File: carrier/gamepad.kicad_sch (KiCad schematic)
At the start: 57 parts, among them SW1 SKRRACE010, SW10 SKRBAAE010, SW11 SW_Push, SW12 SW_DIP_x04, SW2 SKRRACE010, SW3 SKRRACE010, SW4 SKRRACE010, SW5 SKRRACE010, SW6 SKRRACE010, SW7 SKRBAAE010, SW8 SKRBAAE010, SW9 SW_Push, U1 SN74HC14N

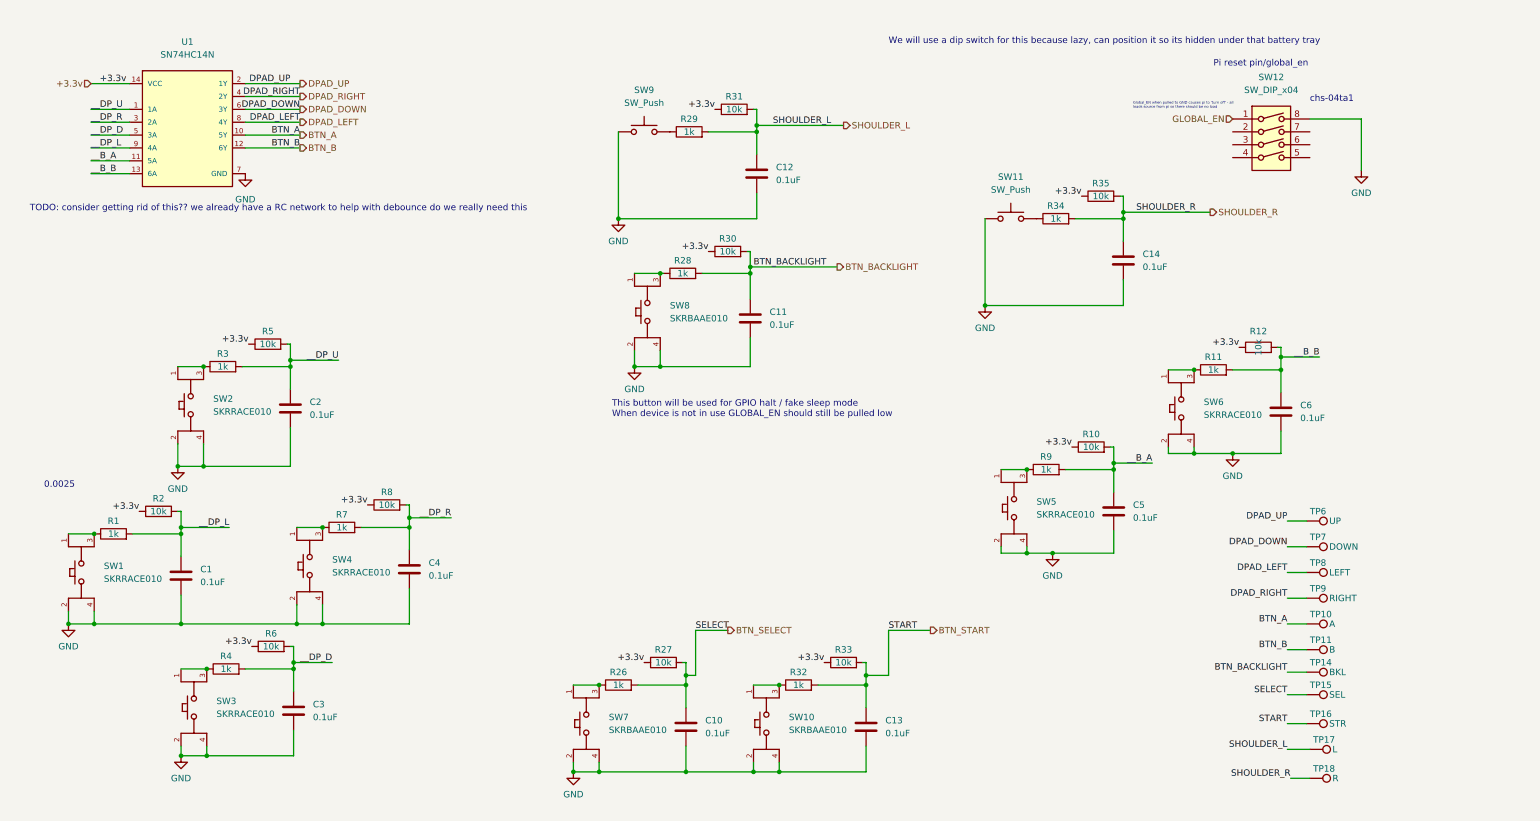
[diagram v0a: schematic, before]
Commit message: getting back into the swing of this
aded some stuff for the resistors, moved some stuff about, removed the schmitt inverter (software is the solution for all our problems, forever)
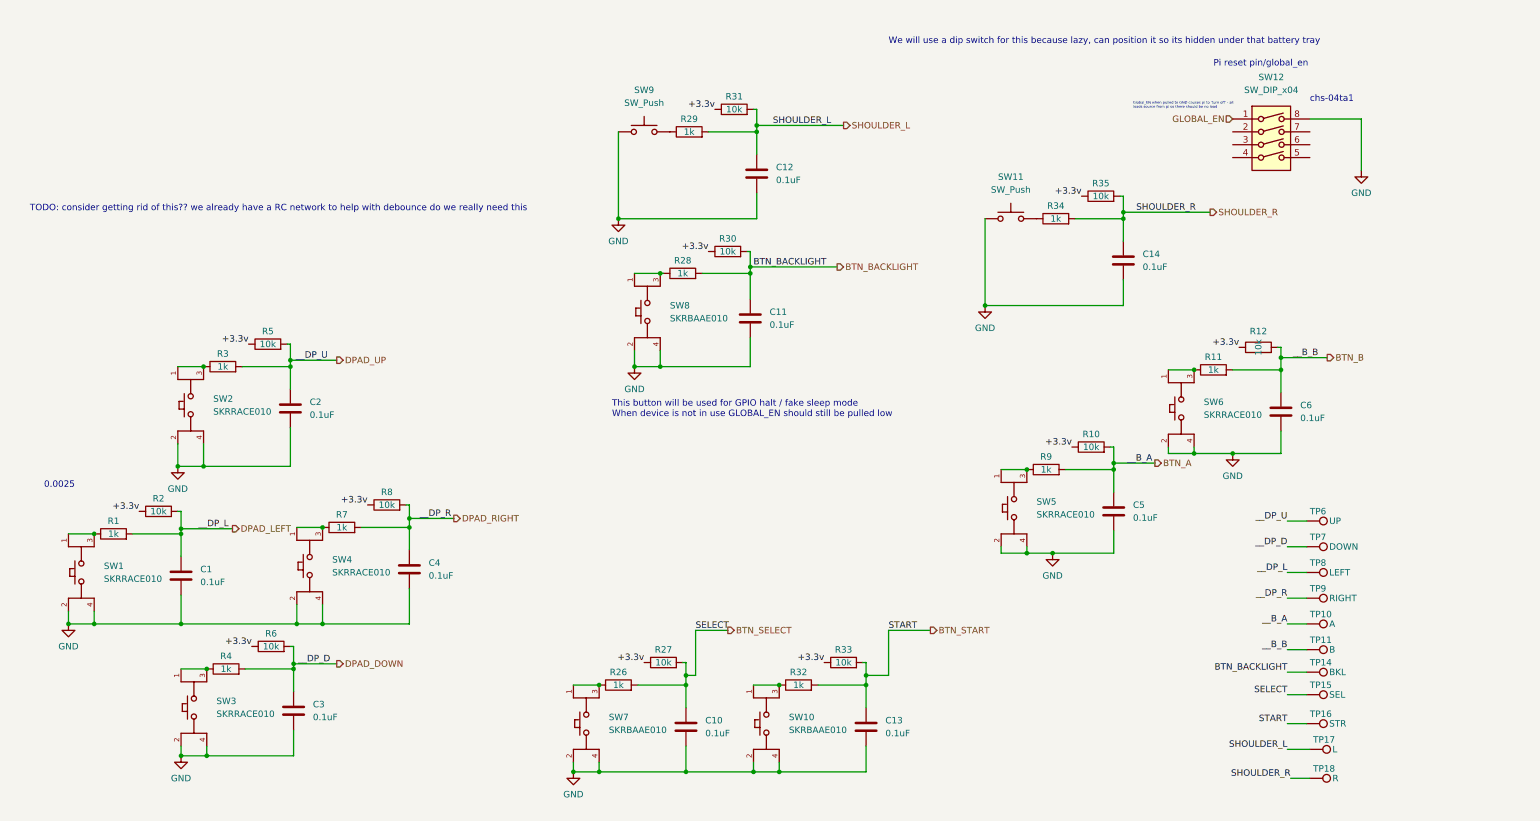
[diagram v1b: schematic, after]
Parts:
- removed U1: SN74HC14N, Package_SO:SO-14_3.9x8.65mm_P1.27mm, symbol TI74HC14N:SN74HC14N
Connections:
- net __B_A is gone; now on net BTN_A: C5.1, R10.2, R9.2
- net __B_B is gone; now on net BTN_B: C6.1, R11.2, R12.2
- net __DP_D is gone; now on net DPAD_DOWN: C3.1, R4.2, R6.2
- net __DP_L is gone; now on net DPAD_LEFT: C1.2, R1.2, R2.2
- net __DP_R is gone; now on net DPAD_RIGHT: C4.1, R7.2, R8.2
- net __DP_U is gone; now on net DPAD_UP: C2.1, R3.2, R5.2

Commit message: Auto stash before merge of "master" and "origin/master"
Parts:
- removed C1, C10, C11, C12, C13, C14, C2, C3, C4, C5, C6: 0.1uF, Capacitor_SMD:C_0402_1005Metric_Pad0.74x0.62mm_HandSolder, symbol Device:C
- removed R1, R11, R26, R28, R29, R3, R32, R34, R4, R7, R9: 1k, Resistor_SMD:R_0402_1005Metric_Pad0.72x0.64mm_HandSolder, symbol Device:R
- removed R10, R12, R2, R27, R30, R31, R33, R35, R5, R6, R8: 10k, Resistor_SMD:R_0402_1005Metric_Pad0.72x0.64mm_HandSolder, symbol Device:R
- removed SW1, SW2, SW3, SW4, SW5, SW6: SKRRACE010, eec:ALPS-SKRRACE010-0-0-MFG, symbol EECBTN:SKRRACE010
- removed SW10, SW7, SW8: SKRBAAE010, eec:SKRBAAE010, symbol EECBTN:SKRBAAE010
- removed SW11, SW9: SW_Push, sw:TE_Connectivity-1-1825027-1-0-0-Recommended_Land_Pattern_, symbol Switch:SW_Push
- removed SW12: SW_DIP_x04, dipswitch:CHS04TA1, symbol Switch:SW_DIP_x04
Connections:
- net BTN_A renamed __B_A
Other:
- note removed: "0.0025"
- note removed: "Global_EN when pulled to GND causes pi to 'turn off' - all loads source from pi so there should be no load"
- note removed: "Pi reset pin/global_en"
- note removed: "We will use a dip switch for this because lazy, can position it so its hidden under that battery tray"
- note removed: "chs-04ta1"

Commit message: a
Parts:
- added C? (x9): 100n, symbol Device:C
- added R? (x9): 1k, symbol Device:R
- added R? (x9): 10k, symbol Device:R
- added SW? (x6): SKRBAAE010, ALPS-SKRRACE010-0-0-*, symbol EECBTN:SKRBAAE010
- added SW? (x3): SKRRACE010, ALPS-SKRRACE010-0-0-*, symbol EECBTN:SKRRACE010
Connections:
- net BTN_B: now also C?.1, R?.2, R?.2
- net BTN_BACKLIGHT: now also C?.1, R?.2, R?.2; no longer TP14.1
- net BTN_SELECT: now also C?.1, R?.2, R?.2; no longer TP15.1
- net BTN_START: now also C?.1, R?.2, R?.2; no longer TP16.1
- net DPAD_DOWN: now also C?.1, R?.2, R?.2
- net DPAD_LEFT: now also C?.1, R?.2, R?.2
- net DPAD_RIGHT: now also C?.1, R?.2, R?.2; no longer TP9.1
- net DPAD_UP: now also C?.1, R?.2, R?.2
- net SHOULDER_L: no longer TP17.1
- net SHOULDER_R: no longer TP18.1
- net __B_A renamed BTN_A
- net BTN_A: now also C?.1, R?.2, R?.2
- new net: R?.1, SW?.3 (x3)
- new net: R?.1, SW?.1, SW?.3 (x6)
- new net: C?.2, SW?.4 (x3)
- new net 3v3: R?.1, R?.1, R?.1, R?.1, R?.1, R?.1, R?.1, R?.1, R?.1
- new net GND: C?.2, C?.2, C?.2, C?.2, C?.2, C?.2, SW?.2, SW?.2, SW?.2, SW?.2, SW?.2, SW?.2, SW?.2, SW?.2, SW?.2, SW?.4, SW?.4, SW?.4, SW?.4, SW?.4, SW?.4
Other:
- note added: "debounce"
- note removed: "TODO: consider getting rid of this?? we already have a RC network to help with debounce do we really need this"
- moved on the sheet: TP10, TP11, TP14, TP15, TP16, TP17, TP18, TP6, TP7, TP8, TP9

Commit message: aa
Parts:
- gave numbers to parts that had none: 36

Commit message: aa
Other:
- note added: "FIND SHOULDER"
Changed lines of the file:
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@@
     (effects (font (size 1.27 1.27)) (justify right bottom))
+  )
+  (text "FIND SHOULDER" (at 178.435 33.02 0)
+    (effects (font (size 2.54 2.54)) (justify left bottom))
   )
   (text "This button will be used for GPIO halt / fake sleep mode\nWhen device is not in use GLOBAL_EN should still be pulled low"

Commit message: thingy
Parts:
- added C?: C, symbol Device:C
- added C? (x2): 100n, symbol Device:C
- added R? (x2): 10k, symbol Device:R
- added R? (x2): 1k, symbol Device:R
- added R?: R, symbol Device:R
- added SW? (x2): SW_Push, panasonic:Panasonic-EVP-AEJB2A-MFG, symbol Switch:SW_Push
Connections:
- net 3v3: now also R?.1, R?.1
- net BTN_BACKLIGHT: now also SW9.1, SW9.3, C?.2, R?.2; no longer C6.1, R11.2, R12.2
- net GND: now also C?.2, C?.2, SW?.1, SW?.1
- net SHOULDER_L: now also TP17.1, C?.1, R?.2, R?.2
- net SHOULDER_R: now also TP18.1, C?.1, R?.2, R?.2
- net at C6.2: no longer SW9.4
- net at R11.1: no longer SW9.3
- new net: C6.1, R11.2, R12.2
- new net: R?.1, SW?.2 (x2)
- new net 5v: C?.1, R?.1
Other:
- note added: "BTN_BACKLIGHT will be reused as POW switch"
- moved on the sheet: C6, R11, R12, SW9, TP17, TP18

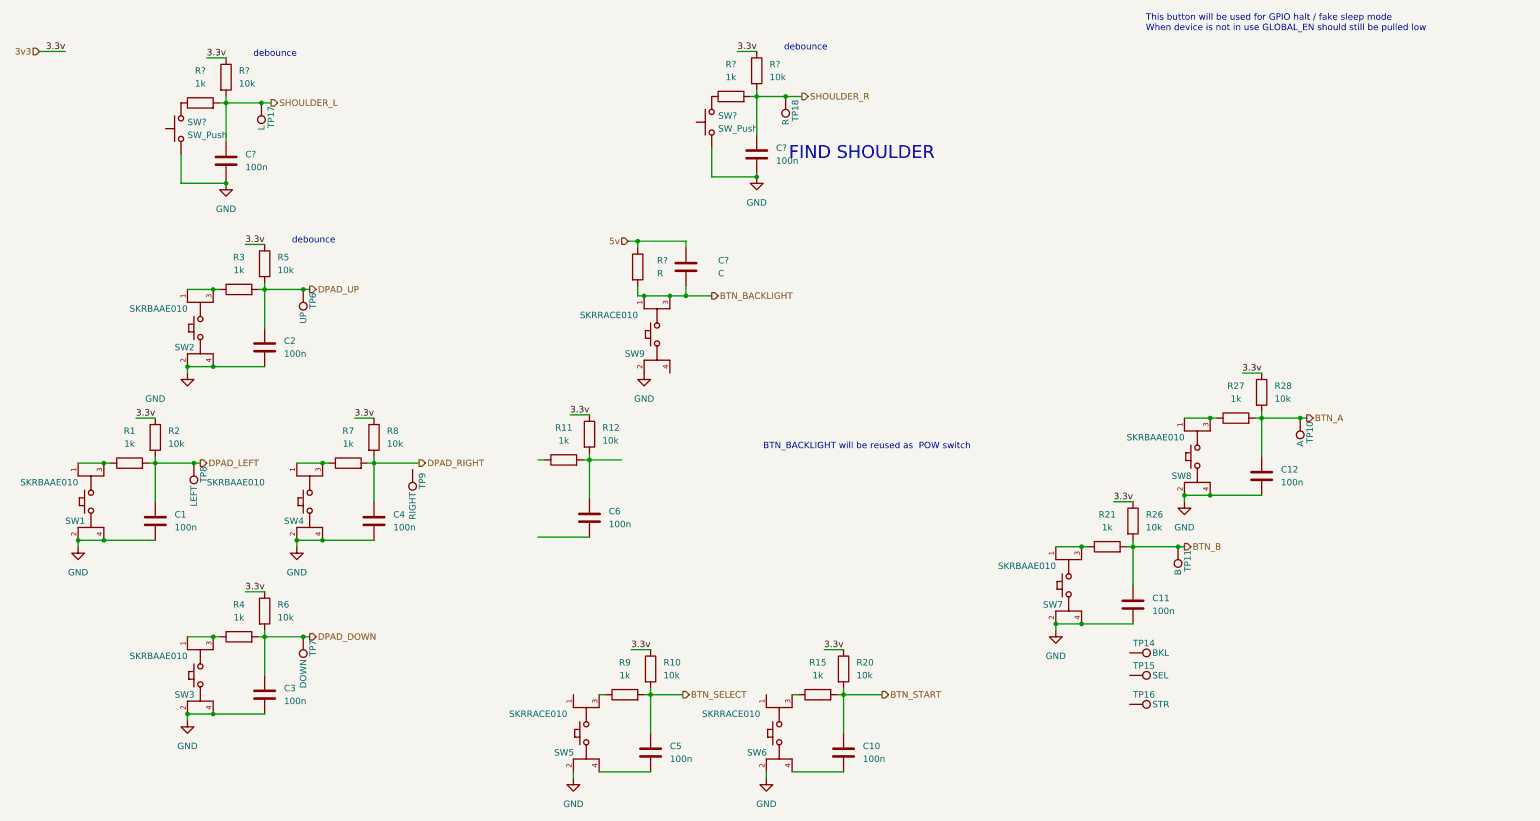
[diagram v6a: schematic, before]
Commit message: fixed switching and added fuel gague
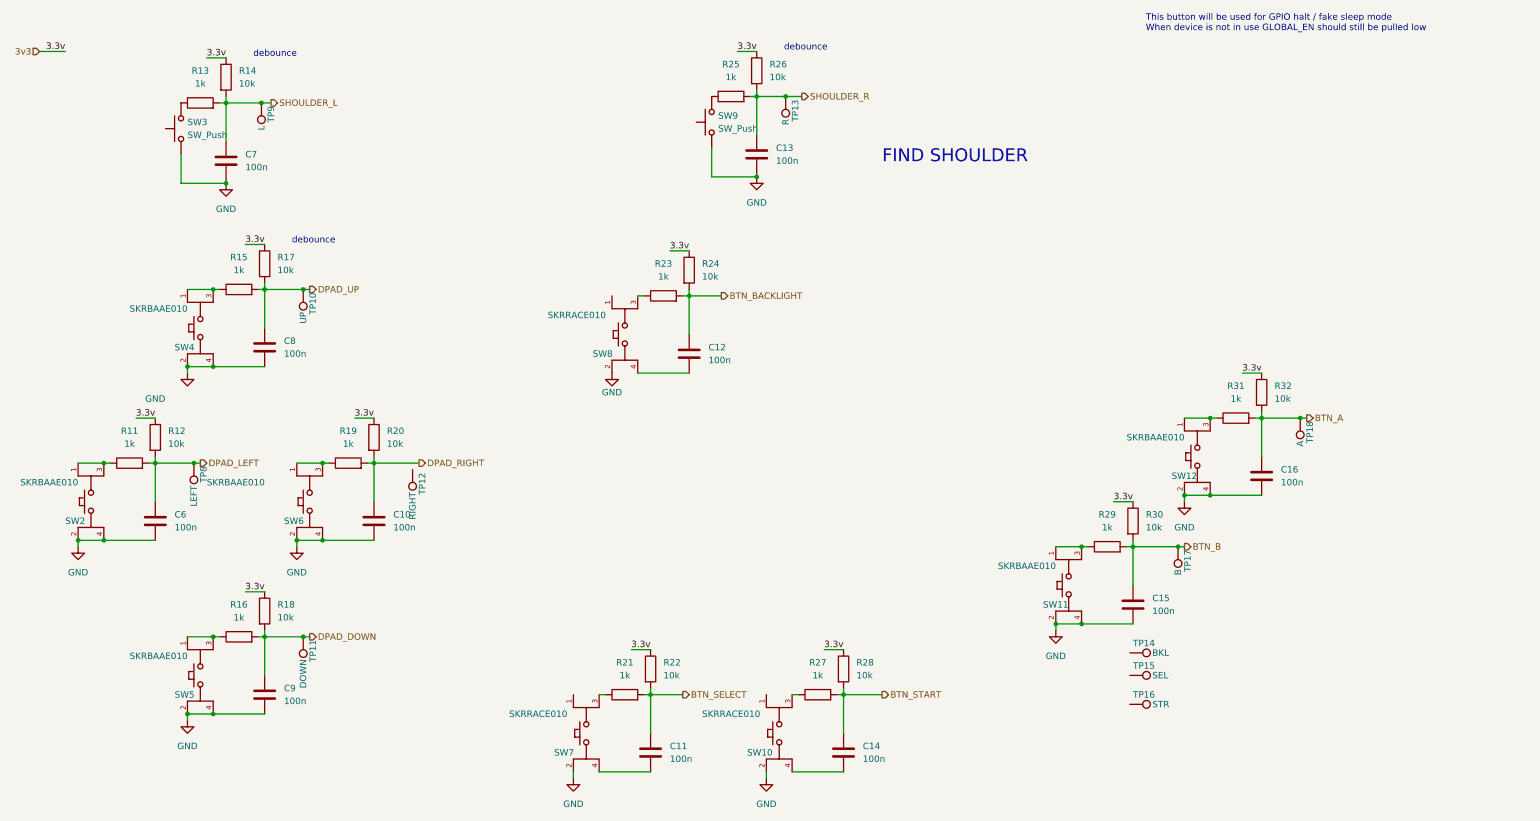
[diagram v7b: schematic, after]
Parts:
- removed C?: C, symbol Device:C
- removed R?: R, symbol Device:R
- gave numbers to parts that had none: 8
- renumbered C4 to C10, C5 to C11, C6 to C12, C10 to C14, C11 to C15, C12 to C16, C1 to C6, C2 to C8, C3 to C9, R1 to R11, R2 to R12, R3 to R15, R4 to R16, R5 to R17, R6 to R18, R7 to R19, R8 to R20, R9 to R21, R10 to R22, R11 to R23, R12 to R24, R15 to R27, R20 to R28, R21 to R29, R26 to R30, R27 to R31, R28 to R32, SW6 to SW10, SW7 to SW11, SW8 to SW12, SW1 to SW2, SW2 to SW4, SW3 to SW5, SW4 to SW6, SW5 to SW7, SW9 to SW8, TP6 to TP10, TP7 to TP11, TP9 to TP12, TP18 to TP13, TP11 to TP17, TP10 to TP18, TP17 to TP9
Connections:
- net BTN_BACKLIGHT: now also C12.1, R23.2, R24.2; no longer SW8.1, SW8.3
- net at C12.2: now also SW8.4
- net at R23.1: now also SW8.3
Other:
- note removed: "BTN_BACKLIGHT will be reused as POW switch"
- moved on the sheet: C12, R23, R24, SW8
